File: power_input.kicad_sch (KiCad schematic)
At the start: 100 parts, among them J201 61300211121, J202 61300211121, J203 61300211121, J204 61300211121, J205 61300211121, J206 61300211121, J207 61300211121, J208 61300211121, Q201 SQ2319CES, Q202 SQ2319CES, Q203 IRFL4315TRPBF, Q204 SQ2319CES, Q205 SQ2319CES, U201 LM4040-5.0, U202 TL331, U203 OPA197, U204 LM4040-5.0, U205 TL331, U206 LM4040-5.0, U207 TL331

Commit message: Move GND-CHASSIS bridge to front page
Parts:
- removed R233: 0 Ω, Resistor_SMD:R_1206_3216Metric, symbol Device:R
- F201: Size (none) -> 2920
- renumbered TP202 to TP201, TP201 to TP202
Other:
- moved on the sheet: TP202

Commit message: Clean up schematics
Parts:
- U201, U204, U206: Zener voltage (none) -> 5 V
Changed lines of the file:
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@@
 	(title_block
 		(title "Linux SBC")
-		(date "2025-12-19")
+		(date "2025-12-26")
 		(rev "v1.0.0")
 	)
@@
 		)
 	)
-	(text_box "- See UVLO.asc for UVLO simulation in LTSPICE.\n- See OVLO.asc for OVLO simulation in LTSPICE.\n- See OCLO.asc for OCLO simulation in LTSPICE.\n- See EMI_FILTER.asc for EMI filter simulation in LTSPICE."
+	(text_box "- See UVLO.asc for UVLO simulation in LTspice.\n- See OVLO.asc for OVLO simulation in LTspice.\n- See OCLO.asc for OCLO simulation in LTspice.\n- See EMI_FILTER.asc for EMI filter simulation in LTspice."
 		(exclude_from_sim no)
 		(at 13.97 260.35 0)
@@
 		)
 	)
-	(text_box "OCLO_IN = I_{IN} * R_{S} * (R_{F} / R_{G}) -> @ 0.1 A = 0.25 V, @ 2 A = 5 V\nV_{CM} = 24 V * (R_{F} / (R_{G} + R_{F})) ~= 23.53 V\nR_{s} Power dissipation = 0.05 * 2 A * 2 A = 0.2 W"
+	(text_box "OCLO_IN = I_{IN} * R_{S} * (R_{F} / R_{G}) -> @ 0.1 A = 0.25 V, @ 2 A = 5 V\nR_{s} power dissipation = 0.05 * 2 A * 2 A = 0.2 W"
 		(exclude_from_sim no)
 		(at 140.97 149.86 0)
@@
 		(dnp no)
 		(property "Reference" "U204"
-			(at 212.344 224.79 90)
+			(at 212.344 224.282 90)
 			(effects
 				(font
@@
 		)
 		(property "Value" "LM4040-5.0"
-			(at 212.344 227.33 90)
+			(at 212.344 226.06 90)
 			(effects
 				(font
@@
 			)
 		)
+		(property "Zener voltage" "5 V"
+			(at 212.598 227.584 90)
+			(effects
+				(font
+					(size 0.7 0.7)
+				)
+				(justify right)
+			)
+		)
 		(pin "2"
 		)
@@
 		(dnp no)
 		(property "Reference" "U206"
-			(at 268.224 106.68 90)
+			(at 268.224 106.172 90)
 			(effects
 				(font
@@
 		)
 		(property "Value" "LM4040-5.0"
-			(at 268.224 109.22 90)
+			(at 268.224 107.95 90)
 			(effects
 				(font
@@
 			)
 		)
+		(property "Zener voltage" "5 V"
+			(at 268.478 109.474 90)
+			(effects
+				(font
+					(size 0.7 0.7)
+				)
+				(justify right)
+			)
+		)
 		(pin "2"
 		)
@@
 	)
 	(symbol
+		(lib_id "Reference_Voltage:LM4040DBZ-5")
+		(at 21.59 228.6 90)
+		(unit 1)
+		(exclude_from_sim no)
+		(in_bom yes)
+		(on_board yes)
+		(dnp no)
+		(property "Reference" "U201"
+			(at 23.114 226.822 90)
+			(effects
+				(font
+					(size 1.27 1.27)
+				)
+				(justify right)
+			)
+		)
+		(property "Value" "LM4040-5.0"
+			(at 23.114 228.6 90)
+			(effects
+				(font
+					(size 1.27 1.27)
+				)
+				(justify right)
+			)
+		)
+		(property "Footprint" "Package_TO_SOT_SMD:SOT-23"
+			(at 26.67 228.6 0)
+			(effects
+				(font
+					(size 1.27 1.27)
+					(italic yes)
+				)
+				(hide yes)
+			)
+		)
+		(property "Datasheet" "https://ww1.microchip.com/downloads/aemDocuments/documents/OTH/ProductDocuments/DataSheets/LM4040-41-Precision-Micropower-Shunt-Voltage-Reference-DS20005757B.pdf"
+			(at 21.59 228.6 0)
+			(effects
+				(font
+					(size 1.27 1.27)
+					(italic yes)
+				)
+				(hide yes)
+			)
+		)
+		(property "Description" "Shunt Voltage Reference IC Fixed 5V V ±1% 15 mA SOT-23-3"
+			(at 21.59 228.6 0)
+			(effects
+				(font
+					(size 1.27 1.27)
+				)
+				(hide yes)
+			)
+		)
+		(property "Digi-Key Part Number" "576-2570-1-ND"
+			(at 21.59 228.6 90)
+			(effects
+				(font
+					(size 1.27 1.27)
+				)
+				(hide yes)
+			)
+		)
+		(property "MPN" "LM4040DYM3-5.0-TR"
+			(at 21.59 228.6 90)
+			(effects
+				(font
+					(size 1.27 1.27)
+				)
+				(hide yes)
+			)
+		)
+		(property "Manufacturer" "Microchip Technology"
+			(at 21.59 228.6 90)
+			(effects
+				(font
+					(size 1.27 1.27)
+				)
+				(hide yes)
+			)
+		)
+		(property "Zener voltage" "5 V"
+			(at 23.368 230.124 90)
+			(effects
+				(font
+					(size 0.7 0.7)
+				)
+				(justify right)
+			)
+		)
+		(pin "2"
+		)
+		(pin "3"
+		)
+		(pin "1"
+		)
+		(instances
+			(project "linux-sbc"
+				(path "/fa11a02f-8043-4153-ab69-88d766503017/524a017a-f4b1-440b-9b41-00cccec69d8d"
+					(reference "U201")
+					(unit 1)
+				)
+			)
+		)
+	)
+	(symbol
 		(lib_id "Connector:TestPoint")
 		(at 62.23 88.9 90)
@@
 					(unit 1)
 				)
-			)
-		)
-	)
-	(symbol
-		(lib_name "LM4040DBZ-5_1")
-		(lib_id "Reference_Voltage:LM4040DBZ-5")
-		(at 21.59 228.6 90)
-		(unit 1)
-		(exclude_from_sim no)
-		(in_bom yes)
-		(on_board yes)
-		(dnp no)
-		(property "Reference" "U201"
-			(at 23.114 227.33 90)
-			(effects
-				(font
-					(size 1.27 1.27)
-				)
-				(justify right)
-			)
-		)
-		(property "Value" "LM4040-5.0"
-			(at 23.114 229.87 90)
-			(effects
-				(font
-					(size 1.27 1.27)
-				)
-				(justify right)
-			)
-		)
-		(property "Footprint" "Package_TO_SOT_SMD:SOT-23"
-			(at 26.67 228.6 0)
-			(effects
-				(font
-					(size 1.27 1.27)
-					(italic yes)
-				)
-				(hide yes)
-			)
-		)
-		(property "Datasheet" "https://ww1.microchip.com/downloads/aemDocuments/documents/OTH/ProductDocuments/DataSheets/LM4040-41-Precision-Micropower-Shunt-Voltage-Reference-DS20005757B.pdf"
-			(at 21.59 228.6 0)
-			(effects
-				(font
-					(size 1.27 1.27)
-					(italic yes)
-				)
-				(hide yes)
-			)
-		)
-		(property "Description" "Shunt Voltage Reference IC Fixed 5V V ±1% 15 mA SOT-23-3"
-			(at 21.59 228.6 0)
-			(effects
-				(font
-					(size 1.27 1.27)
-				)
-				(hide yes)
-			)
-		)
-		(property "Digi-Key Part Number" "576-2570-1-ND"
-			(at 21.59 228.6 90)
-			(effects
-				(font
-					(size 1.27 1.27)
-				)
-				(hide yes)
-			)
-		)
-		(property "MPN" "LM4040DYM3-5.0-TR"
-			(at 21.59 228.6 90)
-			(effects
-				(font
-					(size 1.27 1.27)
-				)
-				(hide yes)
-			)
-		)
-		(property "Manufacturer" "Microchip Technology"
-			(at 21.59 228.6 90)
-			(effects
-				(font
-					(size 1.27 1.27)
-				)
-				(hide yes)
-			)
-		)
-		(pin "2"
-		)
-		(pin "3"
-		)
-		(pin "1"
-		)
-		(instances
-			(project "linux-sbc"
-				(path "/fa11a02f-8043-4153-ab69-88d766503017/524a017a-f4b1-440b-9b41-00cccec69d8d"
-					(reference "U201")
-					(unit 1)
-				)

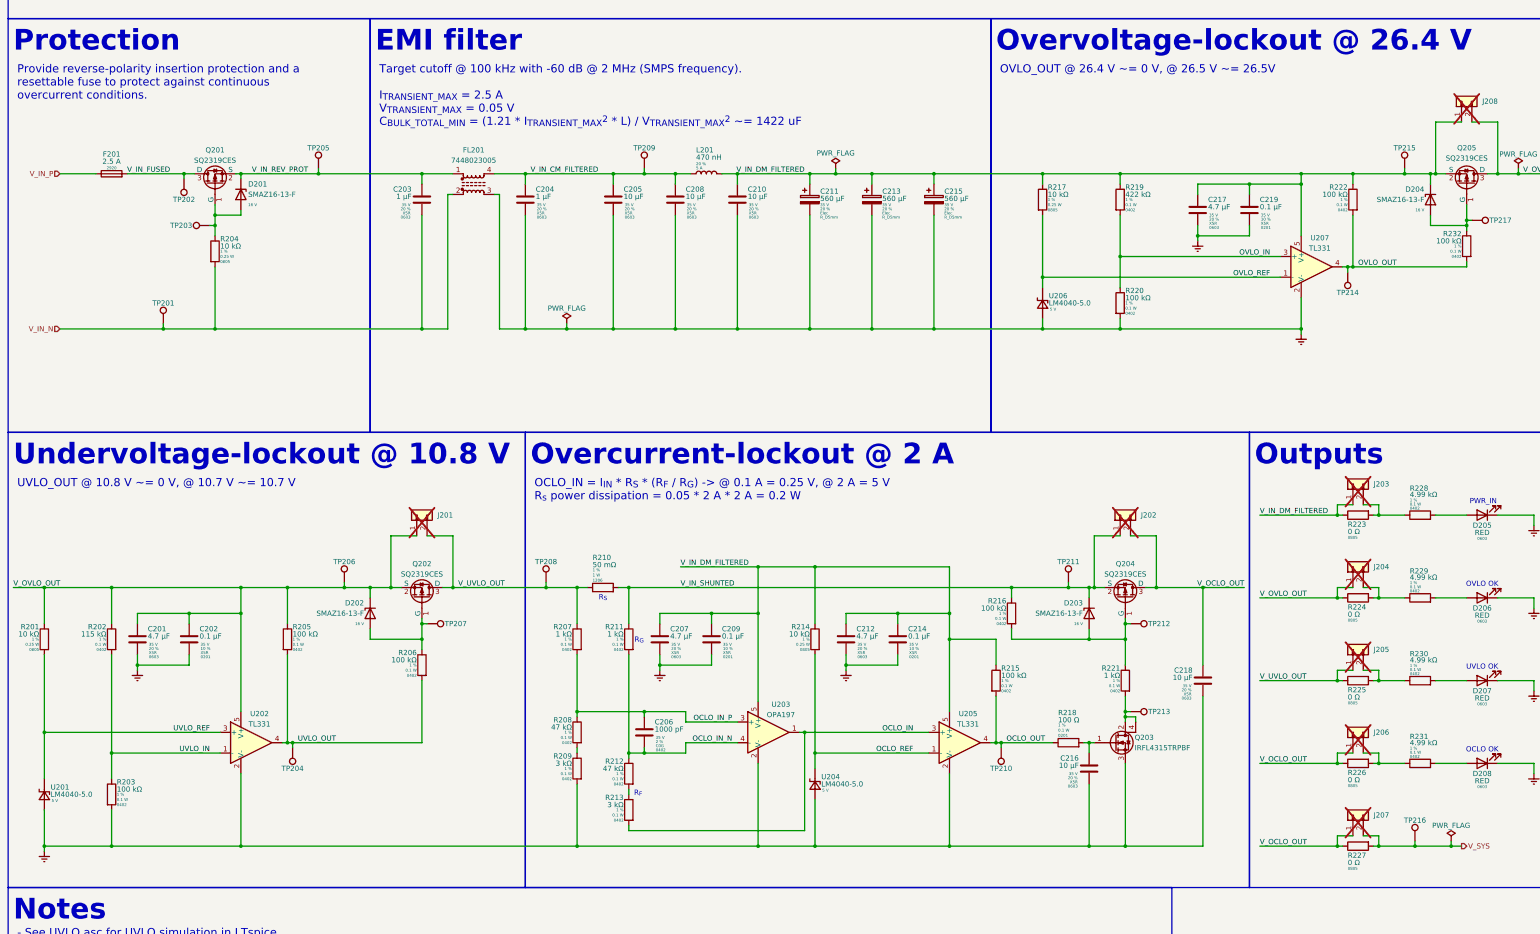
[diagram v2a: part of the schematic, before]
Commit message: Power input: Add hysteresis placeholders
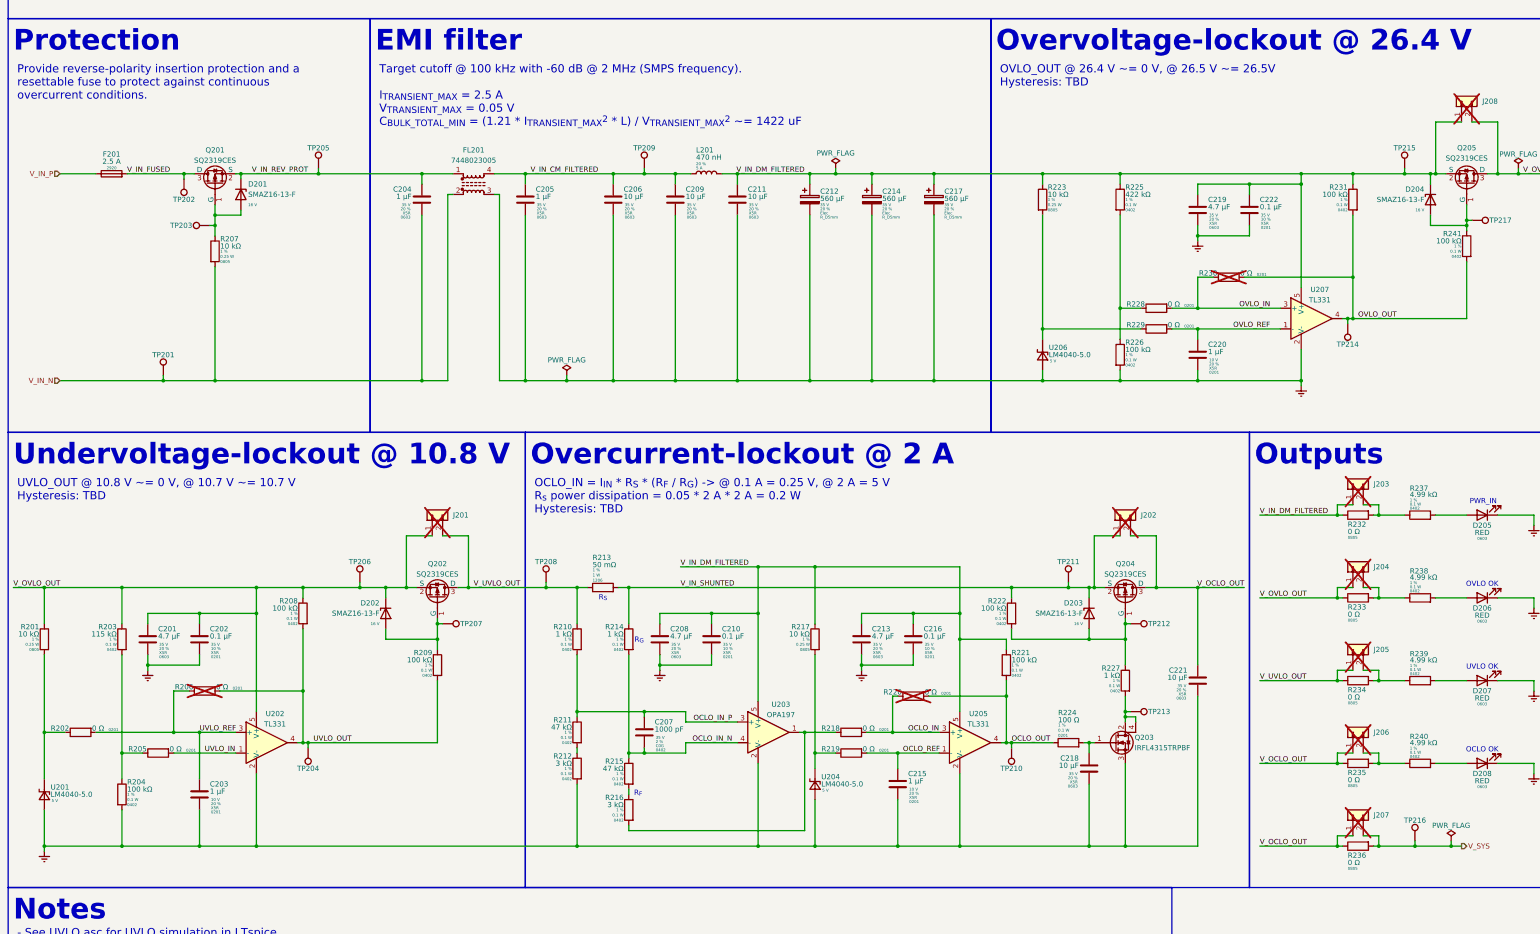
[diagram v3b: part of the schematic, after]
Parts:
- added C203, C215, C220: 1 µF, perfect_footprints:C_0201_0603Metric, symbol Device:C
- added R202, R205, R206, R218, R219, R220, R228, R229, R230: 0 Ω, perfect_footprints:R_0201_0603Metric, symbol Device:R
- renumbered C203 to C204, C204 to C205, C205 to C206, C206 to C207, C207 to C208, C208 to C209, C209 to C210, C210 to C211, C211 to C212, C212 to C213, C213 to C214, C214 to C216, C215 to C217, C216 to C218, C217 to C219, C218 to C221, C219 to C222, R202 to R203, R203 to R204, R204 to R207, R205 to R208, R206 to R209, R207 to R210, R208 to R211, R209 to R212, R210 to R213, R211 to R214, R212 to R215, R213 to R216, R214 to R217, R215 to R221, R216 to R222, R217 to R223, R218 to R224, R219 to R225, R220 to R226, R221 to R227, R222 to R231, R223 to R232, R224 to R233, R225 to R234, R226 to R235, R227 to R236, R228 to R237, R229 to R238, R230 to R239, R231 to R240, R232 to R241
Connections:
- net GND: now also C203.2, C215.2, C220.2
- net OCLO_IN: now also R218.2, R220.1; no longer R216.2, U203.1
- net OCLO_OUT: now also R220.2
- net OCLO_REF: now also C215.1, R219.2; no longer R217.2, U204.1 (K)
- net OVLO_IN: now also R228.2, R230.1; no longer R225.2, R226.1
- net OVLO_OUT: now also R230.2
- net OVLO_REF: now also C220.1, R229.2; no longer R223.2, U206.1 (K)
- net UVLO_IN: now also R205.2; no longer R203.2, R204.1
- net UVLO_OUT: now also R206.2
- net UVLO_REF: now also C203.1, R202.2, R206.1; no longer R201.2, U201.1 (K)
- new net: R201.2, R202.1, U201.1 (K)
- new net: R217.2, R219.1, U204.1 (K)
- new net: R203.2, R204.1, R205.1
- new net: R223.2, R229.1, U206.1 (K)
- new net: R216.2, R218.1, U203.1
- new net: R225.2, R226.1, R228.1
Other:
- moved on the sheet: C201, C202, C213, C216, C221, D202, J201, Q202, R203, R204, R208, R209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

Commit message: Power input: Update PMOSes
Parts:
- removed Q201, Q202, Q204, Q205: SQ2319CES, Package_TO_SOT_SMD:SOT-23, symbol Transistor_FET:Q_PMOS_GSD
- added Q201, Q202, Q204, Q205: DMPH4029LFGQ, Package_SON:Diodes_PowerDI3333-8, symbol Diodes Incorporated:Q_PMOS_DI3333-8
- Q203: value IRFL4315TRPBF -> IRFL4315PbF
- renumbered TP202 to TP201, TP201 to TP202, TP213 to TP212, TP212 to TP213
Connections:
- net V_IN_DM_FILTERED: now also Q205.1 (S), Q205.2 (S), Q205.3 (S)
- net V_IN_FUSED: now also Q201.1 (S), Q201.2 (S), Q201.3 (S)
- net V_IN_REV_PROT: now also Q201.5 (D)
- net V_IN_SHUNTED: now also Q204.1 (S), Q204.2 (S), Q204.3 (S)
- net V_OCLO_OUT: now also Q204.5 (D)
- net V_OVLO_OUT: now also Q202.1 (S), Q202.2 (S), Q202.3 (S), Q205.5 (D)
- net V_UVLO_OUT: now also Q202.5 (D)
- net at D204.2 (A), R241.1, TP217.1: now also Q205.4 (G)
- net at D201.2 (A), R207.1, TP203.1: now also Q201.4 (G)
- net at D203.2 (A), R222.2, R227.1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: now also Q204.4 (G)
- net at D202.2 (A), R209.1, TP207.1: now also Q202.4 (G)
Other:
- moved on the sheet: C221, D201, D202, D203, F201, J201, J208, Q203, R209, R227, R241, TP201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

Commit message: Update power input
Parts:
- added C216: 560 µF, Capacitor_THT:CP_Radial_D5.0mm_P2.00mm, symbol Device:C_Polarized
- D201, D202, D203, D204: value SMAZ16-13-F -> BZT52-C16S; footprint Diode_SMD:D_SMA -> Diode_SMD:D_SOD-323F; Digi-Key Part Number SMAZ16-FDICT-ND -> 3757-BZT52-C16S_R1_00001CT-ND; MPN SMAZ16-13-F -> BZT52-C16S_R1_00001; Manufacturer Diodes Incorporated -> Panjit International Inc.; Size (none) -> SOD-323
- renumbered C209 to C207, C207 to C208, C208 to C209, C211 to C210, C210 to C211, C214 to C213, C217 to C214, C213 to C215, C215 to C217, C216 to C218, C218 to C219, C219 to C220, C220 to C221, C221 to C222, C222 to C223
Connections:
- net GND: now also FL201.2, C216.2; no longer FL201.3
- net V_IN_CM_FILTERED: now also FL201.1; no longer FL201.4
- net V_IN_DM_FILTERED: now also C216.1
- net V_IN_N: now also FL201.3; no longer FL201.2
- net V_IN_REV_PROT: now also FL201.4; no longer FL201.1
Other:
- moved on the sheet: C206, C207, C210, C212, C213, C214, L201, R207, R208, R209, R222, R231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

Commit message: Update 0402 footprints
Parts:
- C208: footprint perfect_footprints:C_0402_1005Metric -> perfect_footprints:C_0402_1005Metric_HDI
- R203, R204, R208, R209, R210, R211, R212, R214, R215, R216, R221, R222, R225, R226, R227, R231, R237, R238, R239, R240, R241: footprint perfect_footprints:R_0402_1005Metric -> perfect_footprints:R_0402_1005Metric_HDI
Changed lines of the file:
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@@
 			)
 		)
-		(property "Footprint" "perfect_footprints:R_0402_1005Metric"
+		(property "Footprint" "perfect_footprints:R_0402_1005Metric_HDI"
 			(at 166.878 223.52 90)
 			(effects
@@
 			)
 		)
-		(property "Footprint" "perfect_footprints:R_0402_1005Metric"
+		(property "Footprint" "perfect_footprints:R_0402_1005Metric_HDI"
 			(at 359.41 202.438 90)
 			(effects
@@
 			)
 		)
-		(property "Footprint" "perfect_footprints:R_0402_1005Metric"
+		(property "Footprint" "perfect_footprints:R_0402_1005Metric_HDI"
 			(at 166.878 190.5 90)
 			(effects
@@
 			)
 		)
-		(property "Footprint" "perfect_footprints:R_0402_1005Metric"
+		(property "Footprint" "perfect_footprints:R_0402_1005Metric_HDI"
 			(at 154.178 213.36 90)
 			(effects
@@
 			)
 		)
-		(property "Footprint" "perfect_footprints:R_0402_1005Metric"
+		(property "Footprint" "perfect_footprints:R_0402_1005Metric_HDI"
 			(at 38.862 228.6 90)
 			(effects
@@
 			)
 		)
-		(property "Footprint" "perfect_footprints:R_0402_1005Metric"
+		(property "Footprint" "perfect_footprints:R_0402_1005Metric_HDI"
 			(at 166.878 232.41 90)
 			(effects
@@
 			)
 		)
-		(property "Footprint" "perfect_footprints:R_0402_1005Metric"
+		(property "Footprint" "perfect_footprints:R_0402_1005Metric_HDI"
 			(at 283.972 120.65 90)
 			(effects
@@
 			)
 		)
-		(property "Footprint" "perfect_footprints:R_0402_1005Metric"
+		(property "Footprint" "perfect_footprints:R_0402_1005Metric_HDI"
 			(at 283.972 82.55 90)
 			(effects
@@
 			)
 		)
-		(property "Footprint" "perfect_footprints:R_0402_1005Metric"
+		(property "Footprint" "perfect_footprints:R_0402_1005Metric_HDI"
 			(at 154.178 190.5 90)
 			(effects
@@
 			)
 		)
-		(property "Footprint" "perfect_footprints:R_0402_1005Metric"
+		(property "Footprint" "perfect_footprints:R_0402_1005Metric_HDI"
 			(at 359.41 182.118 90)
 			(effects
@@
 			)
 		)
-		(property "Footprint" "perfect_footprints:R_0402_1005Metric"
+		(property "Footprint" "perfect_footprints:R_0402_1005Metric_HDI"
 			(at 154.178 222.25 90)
 			(effects
@@
 			)
 		)
-		(property "Footprint" "perfect_footprints:R_0402_1005Metric"
+		(property "Footprint" "perfect_footprints:R_0402_1005Metric_HDI"
 			(at 256.032 196.85 90)
 			(effects
@@
 			)
 		)
-		(property "Footprint" "perfect_footprints:R_0402_1005Metric"
+		(property "Footprint" "perfect_footprints:R_0402_1005Metric_HDI"
 			(at 260.858 182.88 90)
 			(effects
@@
 			)
 		)
-		(property "Footprint" "perfect_footprints:R_0402_1005Metric"
+		(property "Footprint" "perfect_footprints:R_0402_1005Metric_HDI"
 			(at 116.078 193.04 90)
 			(effects
@@
 			)
 		)
-		(property "Footprint" "perfect_footprints:R_0402_1005Metric"
+		(property "Footprint" "perfect_footprints:R_0402_1005Metric_HDI"
 			(at 42.418 190.5 90)
 			(effects
@@
 			)
 		)
-		(property "Footprint" "perfect_footprints:R_0402_1005Metric"
+		(property "Footprint" "perfect_footprints:R_0402_1005Metric_HDI"
 			(at 290.068 196.85 90)
 			(effects
@@
 			)
 		)
-		(property "Footprint" "perfect_footprints:R_0402_1005Metric"
+		(property "Footprint" "perfect_footprints:R_0402_1005Metric_HDI"
 			(at 359.41 222.758 90)
 			(effects
@@
 			)
 		)
-		(property "Footprint" "perfect_footprints:R_0402_1005Metric"
+		(property "Footprint" "perfect_footprints:R_0402_1005Metric_HDI"
 			(at 344.678 81.28 90)
 			(effects
@@
 			)
 		)
-		(property "Footprint" "perfect_footprints:R_0402_1005Metric"
+		(property "Footprint" "perfect_footprints:R_0402_1005Metric_HDI"
 			(at 375.158 91.44 90)
 			(effects
@@
 			)
 		)
-		(property "Footprint" "perfect_footprints:C_0402_1005Metric"
+		(property "Footprint" "perfect_footprints:C_0402_1005Metric_HDI"
 			(at 169.8752 217.17 0)
 			(effects
@@
 			)
 		)
-		(property "Footprint" "perfect_footprints:R_0402_1005Metric"
+		(property "Footprint" "perfect_footprints:R_0402_1005Metric_HDI"
 			(at 359.41 161.798 90)
 			(effects
@@
 			)
 		)
-		(property "Footprint" "perfect_footprints:R_0402_1005Metric"
+		(property "Footprint" "perfect_footprints:R_0402_1005Metric_HDI"
 			(at 86.868 182.88 90)
 			(effects
